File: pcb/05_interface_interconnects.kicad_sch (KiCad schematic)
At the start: 0 parts

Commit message: Added USB and SWD ports with necessary circuitry and ESD protection
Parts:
- added C501, C502: 100nF, FluxNode-FOC:C_0402_1005_DensityHigh, symbol Device:C
- added C503, C504: 100nF 50V, FluxNode-FOC:C_0402_1005_DensityHigh, symbol Device:C
- added D501: PESD4USB3U-TBSX, FluxNode-FOC:PESD4USB3UTBSX, symbol FluxNode-FOC:PESD4USB3U-TBSX
- added J501: XT30PW_2_2_-M.G.B, FluxNode-FOC:AMASS_XT30PW_2_2_-M.G.B, symbol FluxNode-FOC:XT30PW_2_2_-M.G.B
- added J502: Conn_01x08_Pin, Connector_JST:JST_GH_SM08B-GHS-TB_1x08-1MP_P1.25mm_Horizontal, symbol Connector:Conn_01x08_Pin
- added J503: TYPE-C-31-M-12, FluxNode-FOC:HRO_TYPE-C-31-M-12, symbol FluxNode-FOC:TYPE-C-31-M-12
- added J504: SM06B-GHS-TB_LF__SN_, SM06B-GHS-TB_LF__SN_:JST_SM06B-GHS-TB_LF__SN_, symbol FluxNode-FOC:SM06B-GHS-TB_LF__SN_
- added R501, R502: 5k1 1%, FluxNode-FOC:R_0402_1005_DensityHigh, symbol Device:R
- added R503, R504: 100k, FluxNode-FOC:R_0402_1005_DensityHigh, symbol Device:R
- added U501: USBLC6-2SC6, Package_TO_SOT_SMD:SOT-23-6, symbol Power_Protection:USBLC6-2SC6
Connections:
- new net +3V3: C503.1, J504.1
- new net CHASSIS: J503.S1 (SHIELD), J503.S2 (SHIELD), J503.S3 (SHIELD), J503.S4 (SHIELD), J504.S1 (SHIELD), J504.S2 (SHIELD)
- new net D+: J503.A6 (DP1), J503.B6 (DP2), U501.1 (I/O1)
- new net D-: J503.A7 (DN1), J503.B7 (DN2), U501.3 (I/O2)
- new net GND: C501.2, C503.2, C504.2, D501.3 (A), D501.8 (A), J503.A1_B12 (GND), J503.B1_A12 (GND), J504.6, R501.2, R502.2, R504.1, U501.2 (GND)
- new net NRST: C504.1, D501.1 (K), D501.10 (K), J504.5
- new net SWCLK: D501.4 (K), D501.7 (K), J504.3
- new net SWDIO: D501.5 (K), D501.6 (K), J504.2
- new net SWO: D501.2 (K), D501.9 (K), J504.4
- new net USB_CC1: J503.A5 (CC1), R502.1
- new net USB_CC2: J503.B5 (CC2), R501.1
- new net USB_D+: U501.6 (I/O1)
- new net USB_D-: U501.4 (I/O2)
- new net USB_VBUS_SENSE: C501.1, R503.1, R504.2
- new net VBUS: C502.1, J503.A4_B9 (VBUS), J503.B4_A9 (VBUS), R503.2, U501.5 (VBUS)
- no-connect marks 0 -> 2

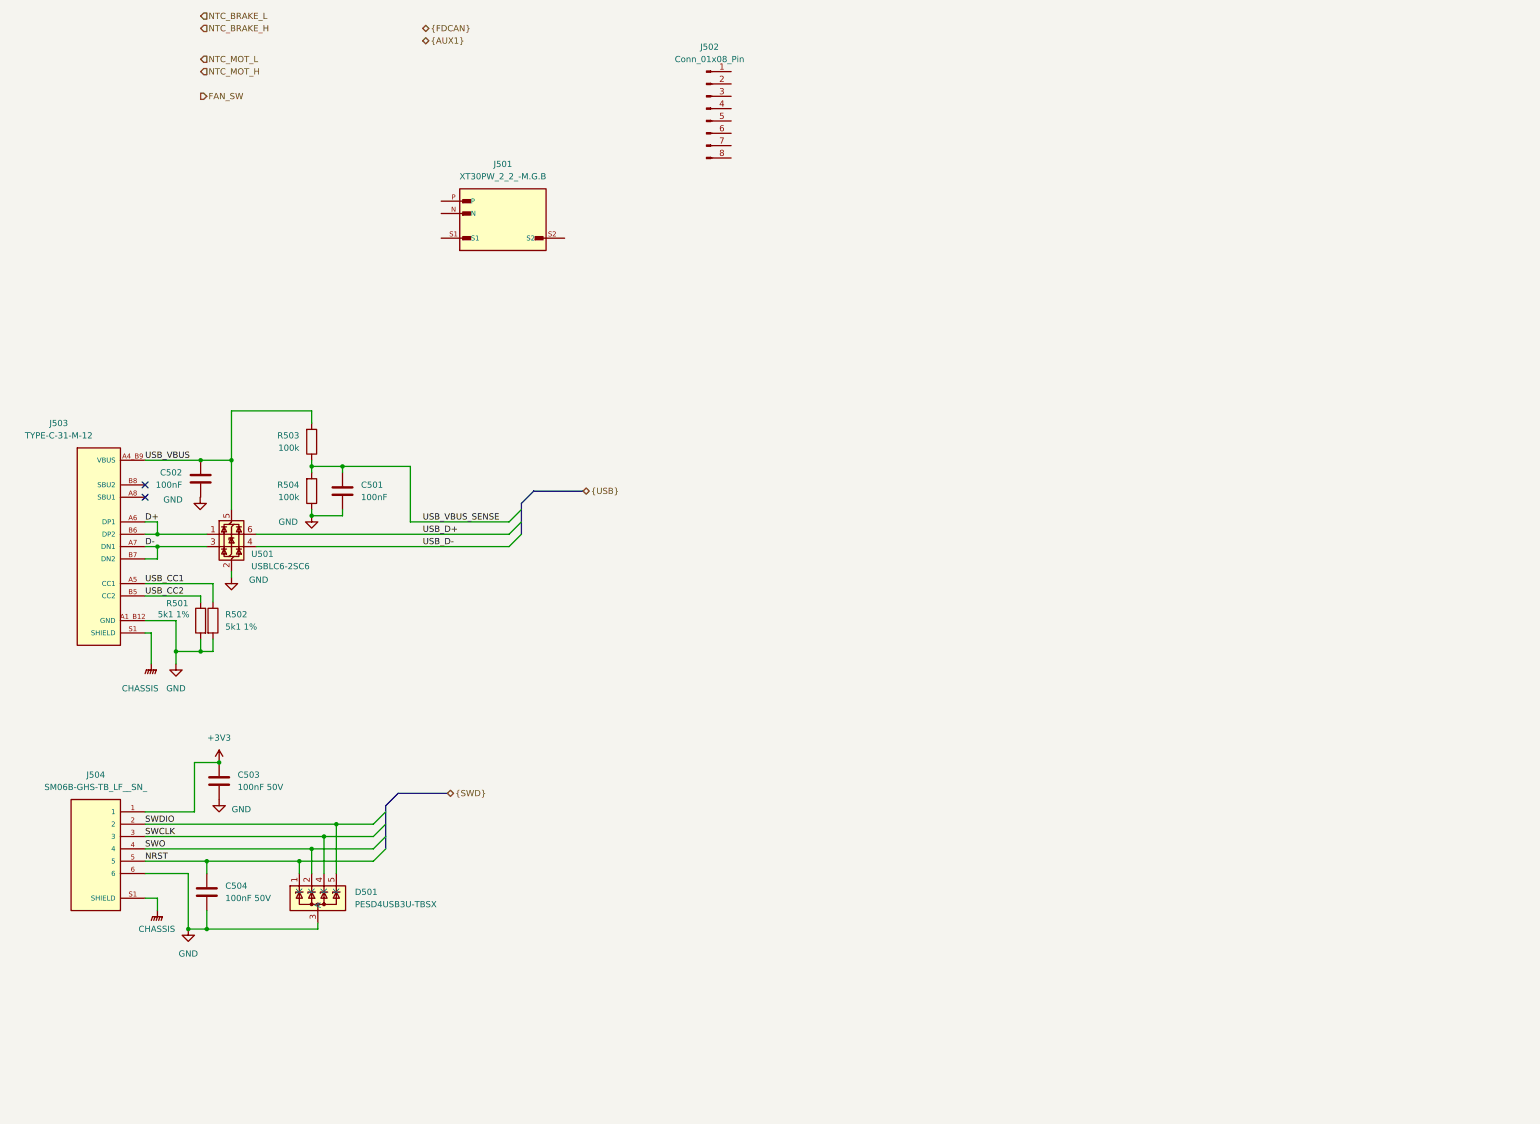
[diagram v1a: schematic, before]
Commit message: Added the XT-30 (2-2) connector for an external brake power resistor and a thermistor
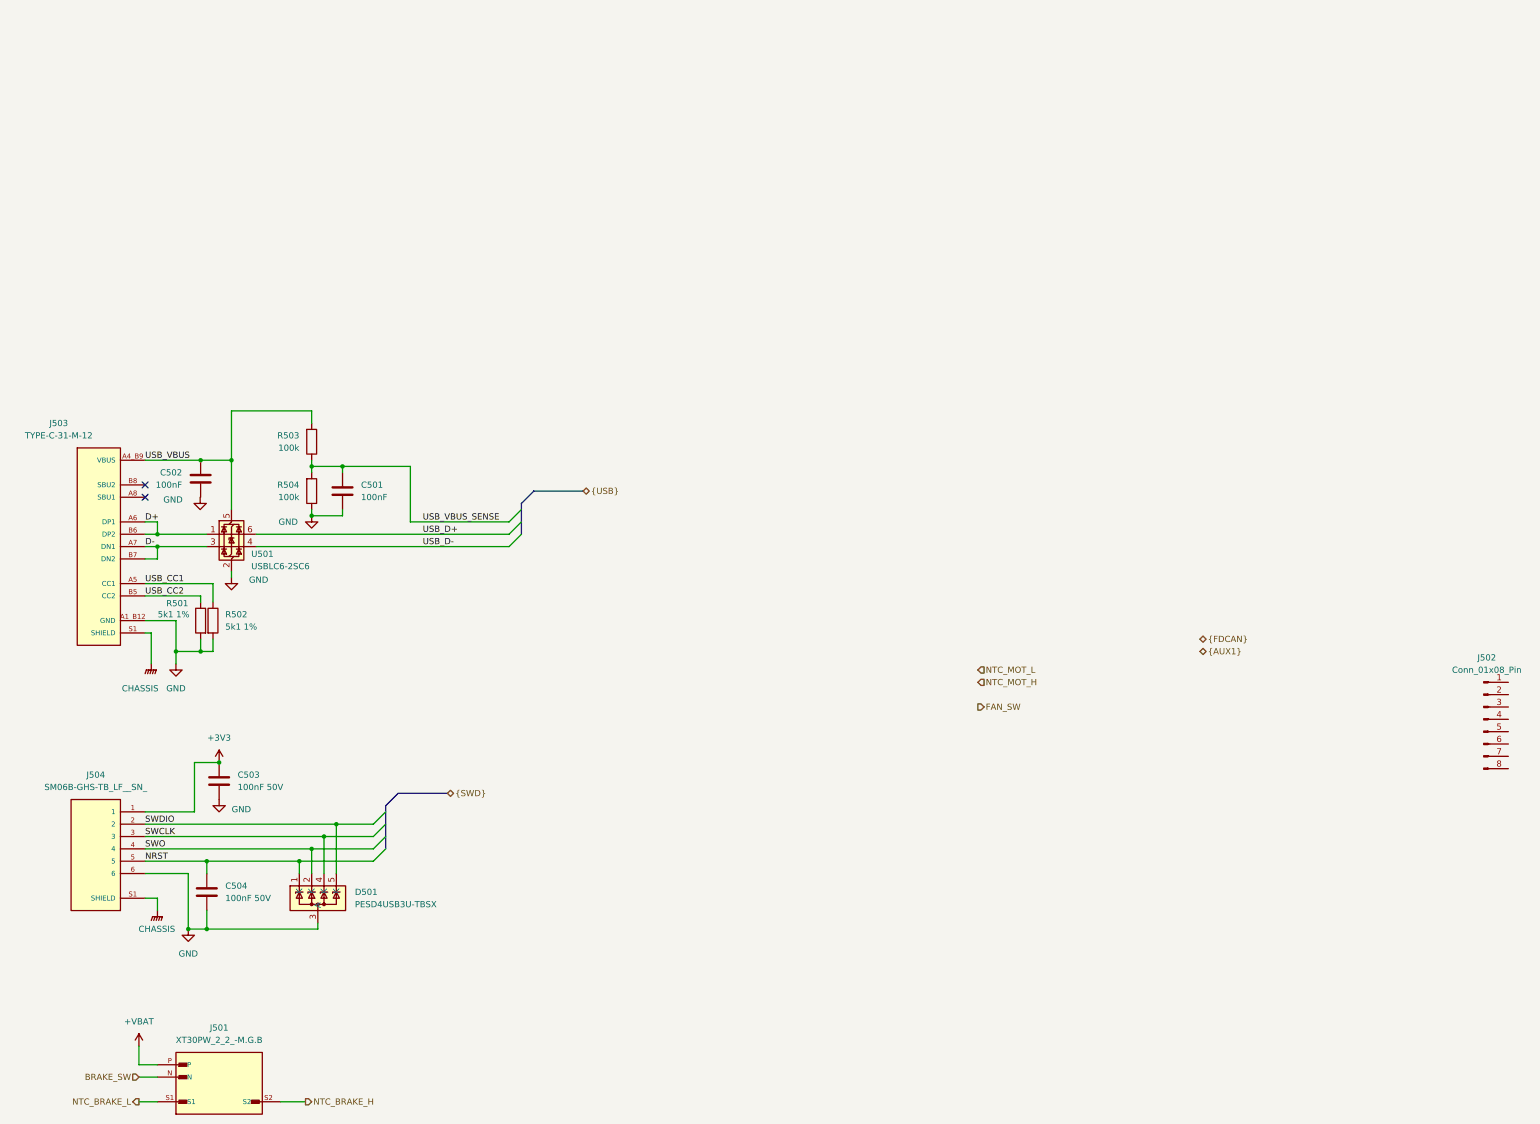
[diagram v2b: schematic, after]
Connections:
- net NTC_BRAKE_H: now also J501.S2
- net NTC_BRAKE_L: now also J501.S1
- net BRAKE_SW: now reaches J501.N
- net +VBAT: now reaches J501.P
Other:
- moved on the sheet: J501, J502
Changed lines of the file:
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@@
 		)
 	)
+	(wire
+		(pts
+			(xy 41.91 147.32) (xy 41.91 151.13)
+		)
+		(stroke
+			(width 0)
+			(type default)
+		)
+	)
 	(bus
 		(pts
@@
 	(wire
 		(pts
+			(xy 41.91 153.67) (xy 45.72 153.67)
+		)
+		(stroke
+			(width 0)
+			(type default)
+		)
+	)
+	(wire
+		(pts
 			(xy 54.61 54.61) (xy 54.61 55.88)
 		)
@@
 	(wire
 		(pts
+			(xy 71.12 158.75) (xy 76.2 158.75)
+		)
+		(stroke
+			(width 0)
+			(type default)
+		)
+	)
+	(wire
+		(pts
 			(xy 77.47 27.94) (xy 77.47 29.21)
 		)
@@
 	(wire
 		(pts
+			(xy 41.91 151.13) (xy 45.72 151.13)
+		)
+		(stroke
+			(width 0)
+			(type default)
+		)
+	)
+	(wire
+		(pts
 			(xy 45.72 44.45) (xy 55.88 44.45)
 		)
@@
 	(wire
 		(pts
+			(xy 41.91 158.75) (xy 45.72 158.75)
+		)
+		(stroke
+			(width 0)
+			(type default)
+		)
+	)
+	(wire
+		(pts
 			(xy 49.53 66.04) (xy 49.53 68.58)
 		)
@@
 	(hierarchical_label "NTC_MOT_L"
 		(shape input)
-		(at 54.61 -55.88 0)
+		(at 214.63 69.85 0)
 		(effects
 			(font
@@
 	)
 	(hierarchical_label "NTC_BRAKE_L"
-		(shape input)
-		(at 54.61 -64.77 0)
+		(shape output)
+		(at 41.91 158.75 180)
 		(effects
 			(font
 				(size 1.27 1.27)
 			)
-			(justify left)
+			(justify right)
 		)
 	)
 	(hierarchical_label "{FDCAN}"
 		(shape bidirectional)
-		(at 100.33 -62.23 0)
+		(at 260.35 63.5 0)
 		(effects
 			(font
@@
 	(hierarchical_label "FAN_SW"
 		(shape output)
-		(at 54.61 -48.26 0)
+		(at 214.63 77.47 0)
 		(effects
 			(font
@@
 	(hierarchical_label "NTC_MOT_H"
 		(shape input)
-		(at 54.61 -53.34 0)
+		(at 214.63 72.39 0)
 		(effects
 			(font
@@
 		)
 	)
+	(hierarchical_label "BRAKE_SW"
+		(shape input)
+		(at 41.91 153.67 180)
+		(effects
+			(font
+				(size 1.27 1.27)
+			)
+			(justify right)
+		)
+	)
 	(hierarchical_label "{AUX1}"
 		(shape bidirectional)
-		(at 100.33 -59.69 0)
+		(at 260.35 66.04 0)
 		(effects
 			(font
@@
 	)
 	(hierarchical_label "NTC_BRAKE_H"
-		(shape input)
-		(at 54.61 -62.23 0)
+		(shape output)
+		(at 76.2 158.75 0)
 		(effects
 			(font
@@
 	(symbol
 		(lib_id "FluxNode-FOC:XT30PW_2_2_-M.G.B")
-		(at 116.84 -24.13 0)
+		(at 58.42 153.67 0)
 		(unit 1)
 		(body_style 1)
@@
 		(fields_autoplaced yes)
 		(property "Reference" "J501"
-			(at 116.84 -34.29 0)
+			(at 58.42 143.51 0)
 			(show_name no)
 			(do_not_autoplace no)
@@
 		)
 		(property "Value" "XT30PW_2_2_-M.G.B"
-			(at 116.84 -31.75 0)
+			(at 58.42 146.05 0)
 			(show_name no)
 			(do_not_autoplace no)
@@
 		)
 		(property "Footprint" "FluxNode-FOC:AMASS_XT30PW_2_2_-M.G.B"
-			(at 116.84 -24.13 0)
+			(at 58.42 153.67 0)
 			(hide yes)
 			(show_name no)
@@
 		)
 		(property "Datasheet" ""
-			(at 116.84 -24.13 0)
+			(at 58.42 153.67 0)
 			(hide yes)
 			(show_name no)
@@
 		)
 		(property "Description" "Industrial Control Plug"
-			(at 116.84 -24.13 0)
+			(at 58.42 153.67 0)
 			(hide yes)
 			(show_name no)
@@
 		)
 		(property "MF" "AMASS"
-			(at 116.84 -24.13 0)
+			(at 58.42 153.67 0)
 			(hide yes)
 			(show_name no)
@@
 		)
 		(property "MAXIMUM_PACKAGE_HEIGHT" "5.2mm"
-			(at 116.84 -24.13 0)
+			(at 58.42 153.67 0)
 			(hide yes)
 			(show_name no)
@@
 		)
 		(property "CREATOR" "ANA"
-			(at 116.84 -24.13 0)
+			(at 58.42 153.67 0)
 			(hide yes)
 			(show_name no)
@@
 		)
 		(property "Price" "None"
-			(at 116.84 -24.13 0)
+			(at 58.42 153.67 0)
 			(hide yes)
 			(show_name no)
@@
 		)
 		(property "Package" "None"
-			(at 116.84 -24.13 0)
+			(at 58.42 153.67 0)
 			(hide yes)
 			(show_name no)
@@
 		)
 		(property "Check_prices" "https://www.snapeda.com/parts/XT30PW(2+2)-M.G.B/AMASS/view-part/?ref=eda"
-			(at 116.84 -24.13 0)
+			(at 58.42 153.67 0)
 			(hide yes)
 			(show_name no)
@@
 		)
 		(property "STANDARD" "Manufacturer Recommendations"
-			(at 118.364 -32.512 0)
+			(at 59.944 145.288 0)
 			(hide yes)
 			(show_name no)
@@
 		)
 		(property "PARTREV" "NA"
-			(at 116.84 -24.13 0)
+			(at 58.42 153.67 0)
 			(hide yes)
 			(show_name no)
@@
 		)
 		(property "VERIFIER" ""
-			(at 116.84 -24.13 0)
+			(at 58.42 153.67 0)
 			(hide yes)
 			(show_name no)
@@
 		)
 		(property "SnapEDA_Link" "https://www.snapeda.com/parts/XT30PW(2+2)-M.G.B/AMASS/view-part/?ref=snap"
-			(at 116.84 -24.13 0)
+			(at 58.42 153.67 0)
 			(hide yes)
 			(show_name no)
@@
 		)
 		(property "MP" "XT30PW(2+2)-M.G.B"
-			(at 116.84 -24.13 0)
+			(at 58.42 153.67 0)
 			(hide yes)
 			(show_name no)
@@
 		)
 		(property "Availability" "Not in stock"
-			(at 116.84 -24.13 0)
+			(at 58.42 153.67 0)
 			(hide yes)
 			(show_name no)
@@
 		)
 		(property "MANUFACTURER" "AMASS"
-			(at 116.84 -24.13 0)
+			(at 58.42 153.67 0)
 			(hide yes)
 			(show_name no)
@@
 	)
 	(symbol
+		(lib_id "FluxNode-FOC:+VBAT")
+		(at 41.91 147.32 0)
+		(unit 1)
+		(body_style 1)
+		(exclude_from_sim no)
+		(in_bom yes)
+		(on_board yes)
+		(in_pos_files yes)
+		(dnp no)
+		(fields_autoplaced yes)
+		(property "Reference" "#PWR0510"
+			(at 41.91 151.13 0)
+			(hide yes)
+			(show_name no)
+			(do_not_autoplace no)
+			(effects
+				(font
+					(size 1.27 1.27)
+				)
+			)
+		)
+		(property "Value" "+VBAT"
+			(at 41.91 142.24 0)
+			(show_name no)
+			(do_not_autoplace no)
+			(effects
+				(font
+					(size 1.27 1.27)
+				)
+			)
+		)
+		(property "Footprint" ""
+			(at 41.91 147.32 0)
+			(hide yes)
+			(show_name no)
+			(do_not_autoplace no)
+			(effects
+				(font
+					(size 1.27 1.27)
+				)
+			)
+		)
+		(property "Datasheet" ""
+			(at 41.91 147.32 0)
+			(hide yes)
+			(show_name no)
+			(do_not_autoplace no)
+			(effects
+				(font
+					(size 1.27 1.27)
+				)
+			)
+		)
+		(property "Description" "Power symbol creates a global label with name \"+VBAT\""
+			(at 41.91 147.32 0)
+			(hide yes)
+			(show_name no)
+			(do_not_autoplace no)
+			(effects
+				(font
+					(size 1.27 1.27)
+				)
+			)
+		)
+		(pin "1"
+		)
+		(instances
+			(project "FluxNode-FOC"
+				(path "/c3755418-04f3-4b36-86ed-bd05a53b8f5f/7f336b96-adfb-4e04-8e5b-99a2af1c766e"
+					(reference "#PWR0510")
+					(unit 1)
+				)
+			)
+		)
+	)
+	(symbol
 		(lib_id "Device:R")
 		(at 54.61 59.69 0)
@@
 	(symbol
 		(lib_id "Connector:Conn_01x08_Pin")
-		(at 158.75 -45.72 0)
+		(at 318.77 80.01 0)
 		(unit 1)
 		(body_style 1)
@@
 		(fields_autoplaced yes)
 		(property "Reference" "J502"
-			(at 159.385 -58.42 0)
+			(at 319.405 67.31 0)
 			(show_name no)
 			(do_not_autoplace no)
@@
 		)
 		(property "Value" "Conn_01x08_Pin"
-			(at 159.385 -55.88 0)
+			(at 319.405 69.85 0)
 			(show_name no)
 			(do_not_autoplace no)
@@
 		)
 		(property "Footprint" "Connector_JST:JST_GH_SM08B-GHS-TB_1x08-1MP_P1.25mm_Horizontal"
-			(at 158.75 -45.72 0)
+			(at 318.77 80.01 0)
 			(hide yes)
 			(show_name no)
@@
 		)
 		(property "Datasheet" ""
-			(at 158.75 -45.72 0)
+			(at 318.77 80.01 0)
 			(hide yes)
 			(show_name no)
@@
 		)
 		(property "Description" "Generic connector, single row, 01x08, script generated"
-			(at 158.75 -45.72 0)
+			(at 318.77 80.01 0)
 			(hide yes)
 			(show_name no)

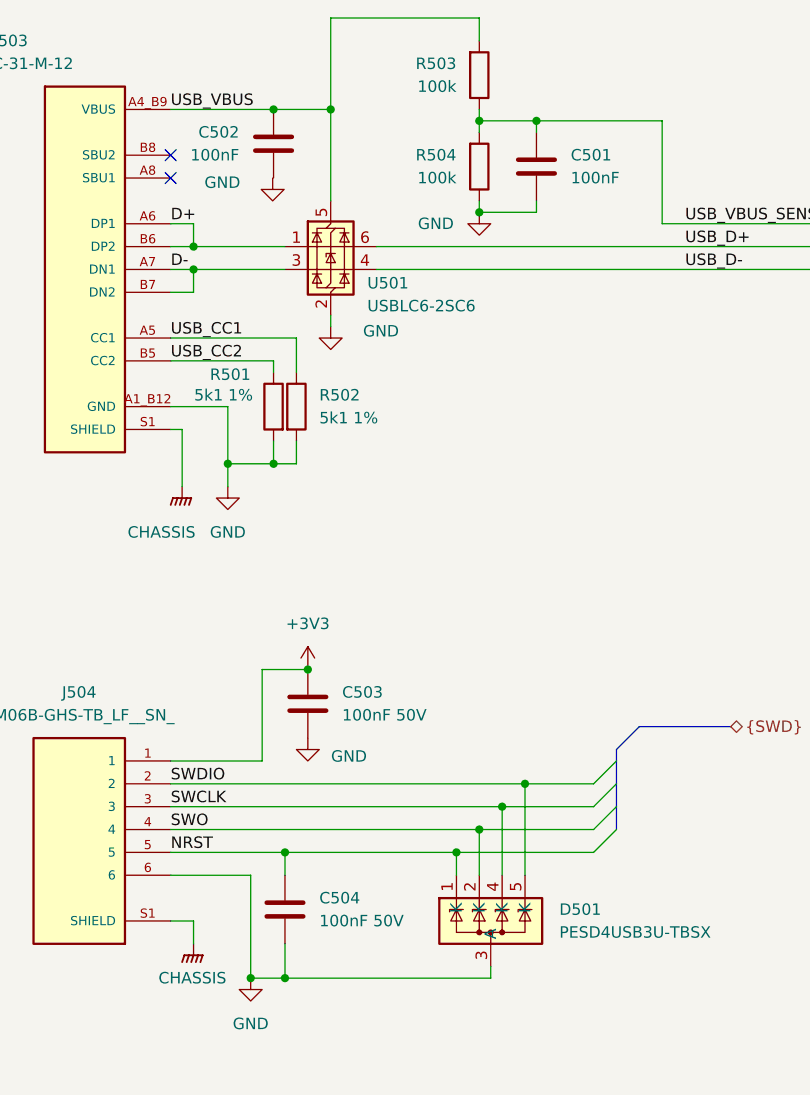
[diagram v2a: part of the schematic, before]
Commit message: Unified all different LCSC part numbers of the same exact components to just one variant
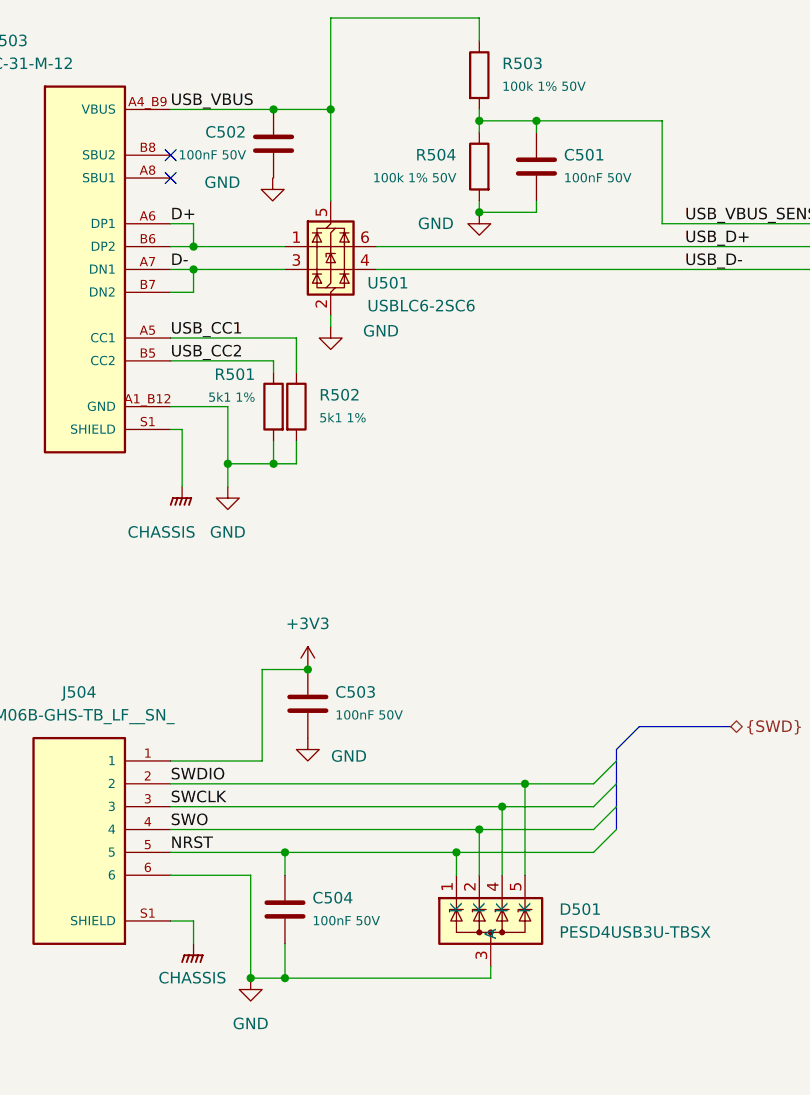
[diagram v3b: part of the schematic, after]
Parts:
- C501, C502: value 100nF -> 100nF 50V; LCSC (none) -> C361198; MPN (none) -> C1005X7R1H104KT000F
- C503, C504: LCSC (none) -> C361198; MPN (none) -> C1005X7R1H104KT000F
- D501: Mouser Part Number 771-PESD4USB3U-TBSX -> (none); Mouser Price/Stock https://www.mouser.co.uk/ProductDetail/Nexperia/PESD4USB3U-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 -> (none)
- J501: Availability Not in stock -> (none); CREATOR ANA -> (none); Check_prices https://www.snapeda.com/parts/XT30PW(2+2)-M.G.B/AMASS/view-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 -> (none); LCSC (none) -> C19268030; MP XT30PW(2+2)-M.G.B -> (none); MPN (none) -> XT30PW(2+2)-M.G.B; PARTREV NA -> (none); Package None -> (none); Price None -> (none); STANDARD Manufacturer Recommendations -> (none); SnapEDA_Link https://www.snapeda.com/parts/XT30PW(2+2)-M.G.B/AMASS/view-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 -> (none)
- J504: footprint SM06B-GHS-TB_LF__SN_:JST_SM06B-GHS-TB_LF__SN_ -> FluxNode-FOC:JST_SM06B-GHS-1.25mm-Horizontal; Availability In Stock -> (none); Check_prices https://www.snapeda.com/parts/SM06B-GHS-TB(LF)(SN)/JST/view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 -> (none); LCSC (none) -> C225129; MF JST Sales America Inc. -> (none); MP SM06B-GHS-TB(LF)(SN) -> (none); MPN (none) -> A1257WR-S-6P; PARTREV N/A -> (none); Package None -> (none); Price None -> (none); STANDARD Manufacturer Recommendations -> (none); SnapEDA_Link https://www.snapeda.com/parts/SM06B-GHS-TB(LF)(SN)/JST/view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 -> (none)
- R501, R502: LCSC (none) -> C482212; MPN (none) -> CRCW04025K10FKED
- R503, R504: value 100k -> 100k 1% 50V; LCSC (none) -> C728576; MPN (none) -> RT0402FRE07100KL
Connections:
- net GND: now also R504.2; no longer R504.1
- net USB_VBUS_SENSE: now also R503.2, R504.1; no longer R503.1, R504.2
- net VBUS: now also R503.1; no longer R503.2
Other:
- company: (none) -> PhiMai

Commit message: Utilized new connector footprint
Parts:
- J501: footprint FluxNode-FOC:AMASS_XT30PW_2_2_-M.G.B -> FluxNode-FOC:AMASS_XT30PW-M_2x2_P5.0mm_Horizontal
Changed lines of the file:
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@@
 			)
 		)
-		(property "Footprint" "FluxNode-FOC:AMASS_XT30PW_2_2_-M.G.B"
+		(property "Footprint" "FluxNode-FOC:AMASS_XT30PW-M_2x2_P5.0mm_Horizontal"
 			(at 58.42 153.67 0)
 			(hide yes)
